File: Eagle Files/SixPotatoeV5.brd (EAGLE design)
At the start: 120 x 60 mm, 27 parts, among them J3 IMU, J4 ON/OFF, J5 GND, J6 3.3v

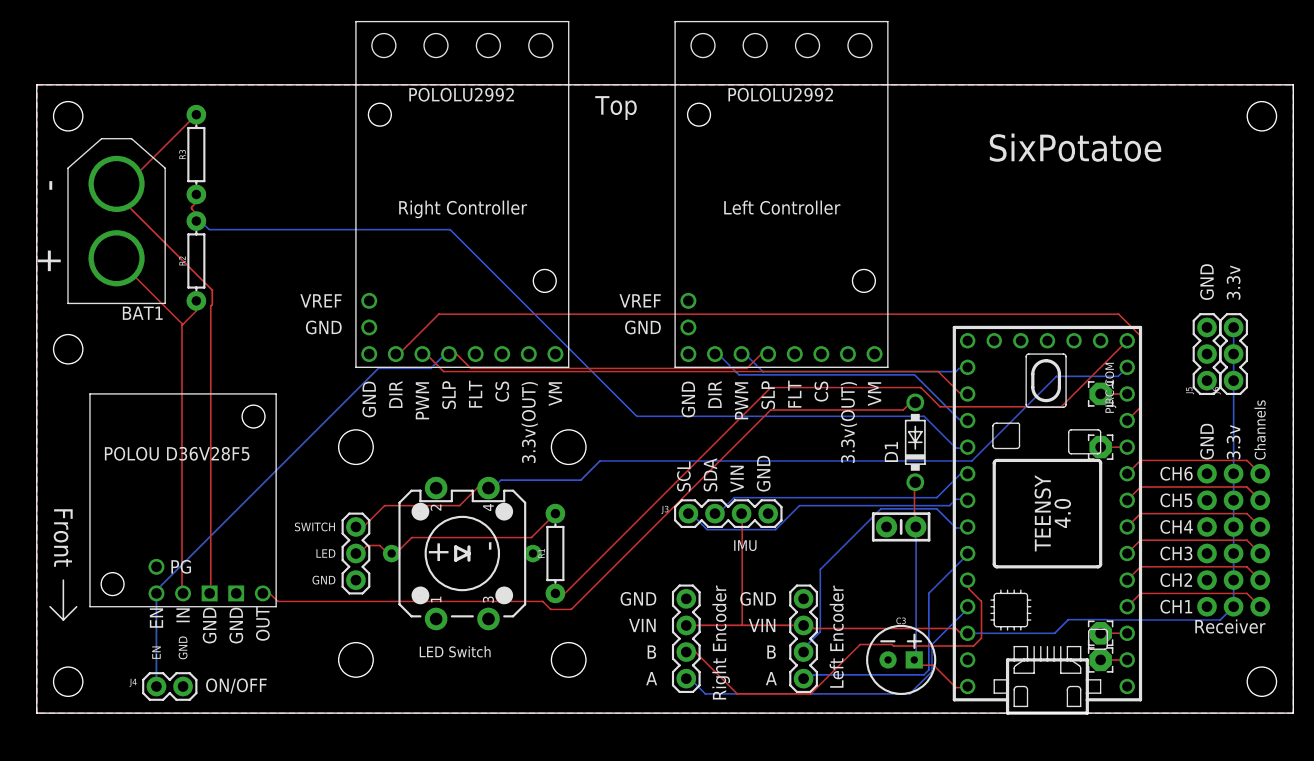
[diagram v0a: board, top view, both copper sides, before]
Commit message: Video completed
Also, excess code removed, first routes checked out.
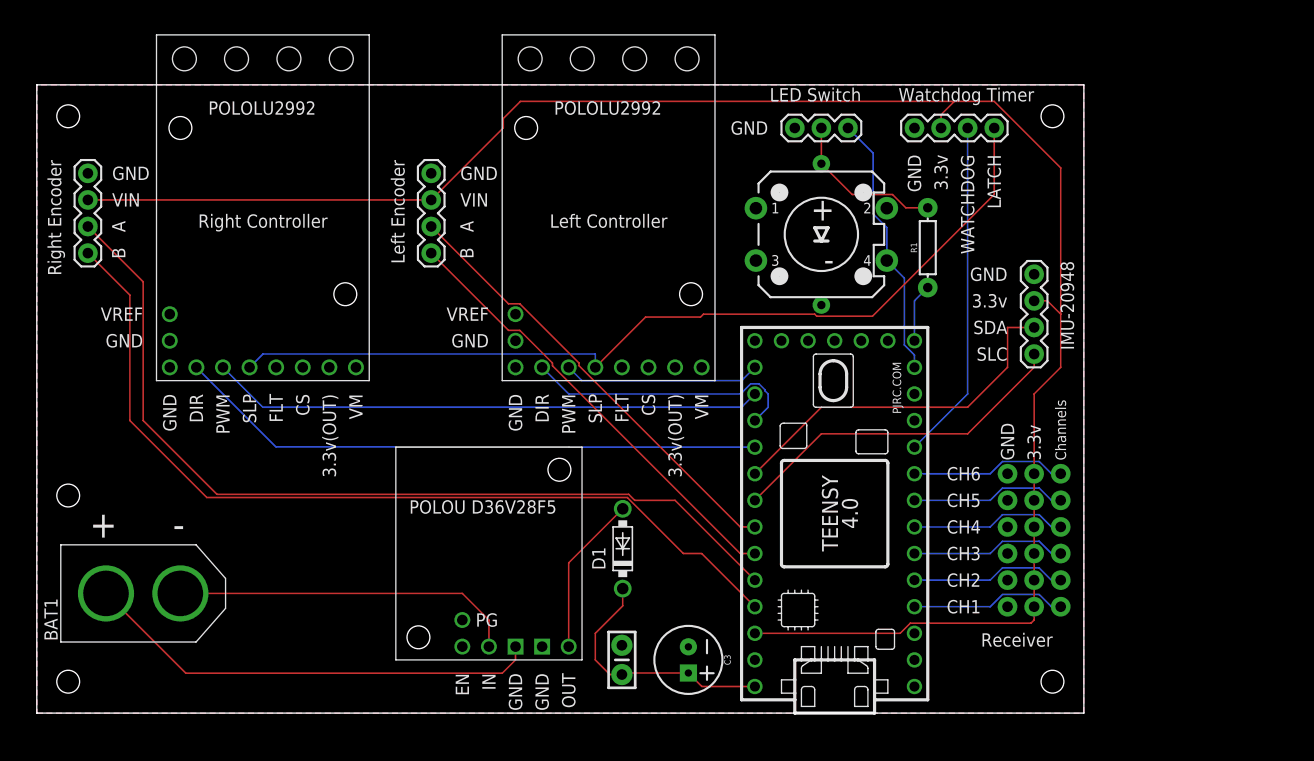
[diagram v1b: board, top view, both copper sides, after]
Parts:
- removed 0, 1, 10, 8: (no value), wirepad:2,15/1,0
- removed J4: ON/OFF, SparkFun-Connectors:1X02
- removed J5: GND, SparkFun-Connectors:1X03
- removed J6: 3.3v, SparkFun-Connectors:1X03
- removed R2, R3: 15k, SparkFun-Resistors:AXIAL-0.3
- removed U$5: SEN15335_NO_PTH, TimEagleLibrary:SEN15335_NO_PTH
- added J7: (no value), SparkFun-Connectors:1X04
- J3: value IMU -> (none)
- moved J1 70.1 mm to (4.88, 51.5)
- moved J19 60.5 mm to (77.5, 55.9), turned to 180 degrees
- moved J2 54.0 mm to (37.7, 51.5)
- moved R1 46.0 mm to (85.1, 44.5)
- moved S2 45.9 mm to (74.9, 45.7), turned to 0 degrees
- moved J3 40.2 mm to (95.2, 41.9), turned to 270 degrees
- moved BAT1 35.7 mm to (10.2, 11.4), turned to 180 degrees
- moved D1 29.7 mm to (56.0, 15.7)
- moved U$4 29.6 mm to (43.2, 14.0)
- moved C2 29.5 mm to (55.9, 5.08), turned to 270 degrees
- moved C3 20.3 mm to (62.2, 5.08), turned to 270 degrees
- moved U$1 20.3 mm to (76.2, 19.1)
- moved U$3 19.1 mm to (31.8, 64.8)
- moved J10 19.1 mm to (92.7, 10.2)
- moved J8 19.0 mm to (97.8, 10.2)
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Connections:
- removed net ENABLE: J4.1, U$2.SLP, U$3.SLP, U$4.EN
- removed net N$1: 0.1, U$1.0/RX
- removed net N$5: 1.1, U$1.1/TX
- removed net N$6: 10.1, U$1.10/CS
- removed net N$7: 8.1, U$1.8
- removed net VMON: R2.P$2, R3.P$1, U$1.17/A3
- new net LATCH: J7.4, U$2.SLP, U$3.SLP
- new net WATCHDOG: J7.3, U$1.8
- net 3.3V: now also J3.2, J7.2; no longer J3.3, J6.1, J6.2, J6.3
- net DIR_RIGHT: now also U$1.17/A3; no longer U$1.9/CS
- net GND: now also J3.1, J7.1; no longer J3.4, J4.2, J5.1, J5.2, J5.3
- net GND2: now also BAT1.+; no longer BAT1.-, R3.P$2
- net SCL: now also J3.4; no longer J3.1
- net SDA: now also J3.3; no longer J3.2
- net VBATT: now also BAT1.-; no longer BAT1.+, R2.P$1
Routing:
- net 3.3V: track 91.1 -> 177.5 mm
- net LATCH: track 0.00 -> 86.3 mm
- net VMON: track 85.7 -> 0.00 mm
- net ENABLE: track 78.1 -> 0.00 mm
- net N$3: track 66.1 -> 5.61 mm
- net 5V: track 71.1 -> 15.3 mm
- net N$4: track 80.0 -> 25.5 mm
- net A_RIGHT: track 32.5 -> 84.7 mm
- net B_RIGHT: track 38.3 -> 85.4 mm
- net WATCHDOG: track 0.00 -> 32.6 mm
- net DIR_RIGHT: track 82.2 -> 56.5 mm
- net A_LEFT: track 25.0 -> 42.9 mm
- net B_LEFT: track 25.8 -> 42.9 mm
- net GND2: track 53.5 -> 44.1 mm
- net SDA: track 25.7 -> 34.7 mm
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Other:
- board size 120 x 60 mm -> 100 x 60 mm
- board text added: "A (Yellow)"
- board text added: "B (Brown)"
- board text added: "GND (Green)"
- board text added: "LATCH"
- board text added: "SLC"
- board text added: "VIN (Orange)"
- board text added: "WATCHDOG"
- board text added: "Watchdog Timer"
- board text removed: "0"
- board text removed: "1"
- board text removed: "10"
- board text removed: "8"
- board text removed: "Bottom"
- board text removed: "Front"
- board text removed: "IMU"
- board text removed: "LED"
- board text removed: "ON/OFF"
- board text removed: "SCL"
- board text removed: "SWITCH"
- board text removed: "SixPotatoe"
- board text removed: "Top"
